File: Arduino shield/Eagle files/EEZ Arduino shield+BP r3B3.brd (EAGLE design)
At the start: 207 x 74 mm, 181 parts, among them IC21 TLC5925IDBQR, IC22 Si8641EC-B-IS1, IC23 SI8651EC-B-IS1, IC24 SI8651EC-B-IS1, IC25 LD1117ADT33TR, IC26 Si8641EC-B-IS1, IC27 PCA21125, IC28 AT25256B, IC29 W5500, IC30 BC857BS, IC31 TLC555, IC32 SN74LVC2G08DCTR, IC33 TPS3705-33D, IC34 SN74LV1T34DBVR, IC35 SN74LVC2G02DCTR, J1 BS-244DSM-R, J2 BS-244DSM-G, J3 BS-244DSM-B, J4 BS-244DSM-R, J5 BS-244DSM-B, Q23 IRLML2246TRPBF, Q24 IRLML2246TRPBF, Q25 IRLML2246TRPBF, Q26 IRLML2246TRPBF, Q27 2N7002, Q28 IRLML2246TRPBF, Q29 2N7002, Q30 2N7002, SW1 A101SYCQ04, SW2 1301.9316, X12 MC000006, X13 TSW-113-07-F-D, X14 MC000005, X15 TSW-113-07-F-D, X16 09185067324, X17 22-23-2021, X18 826629-8, X19 22-23-2041, X20 SSW-105-02-S-D, Y1 32,768kHz, Y2 25MHz

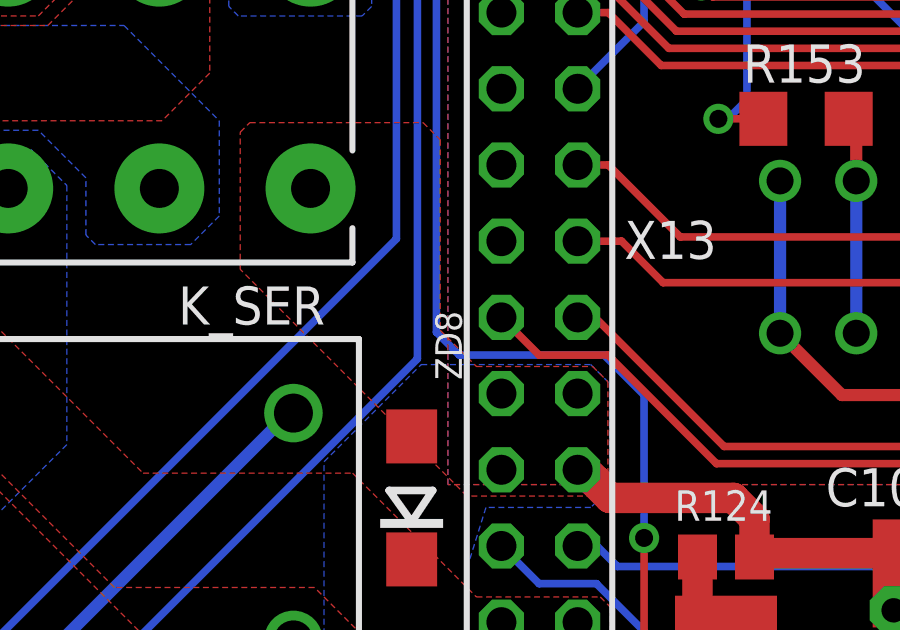
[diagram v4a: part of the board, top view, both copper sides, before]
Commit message: Missed hole added to Power board, minor bottom silk mask changes
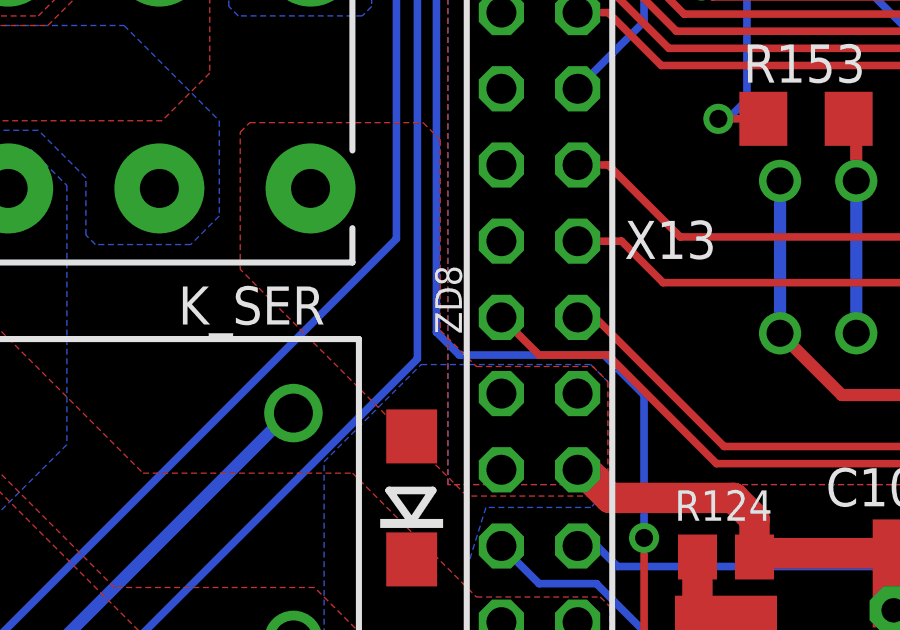
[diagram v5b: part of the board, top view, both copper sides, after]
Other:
- board text removed: "Licensed under the TAPR Open Hardware License (www.tapr.org/OHL)"

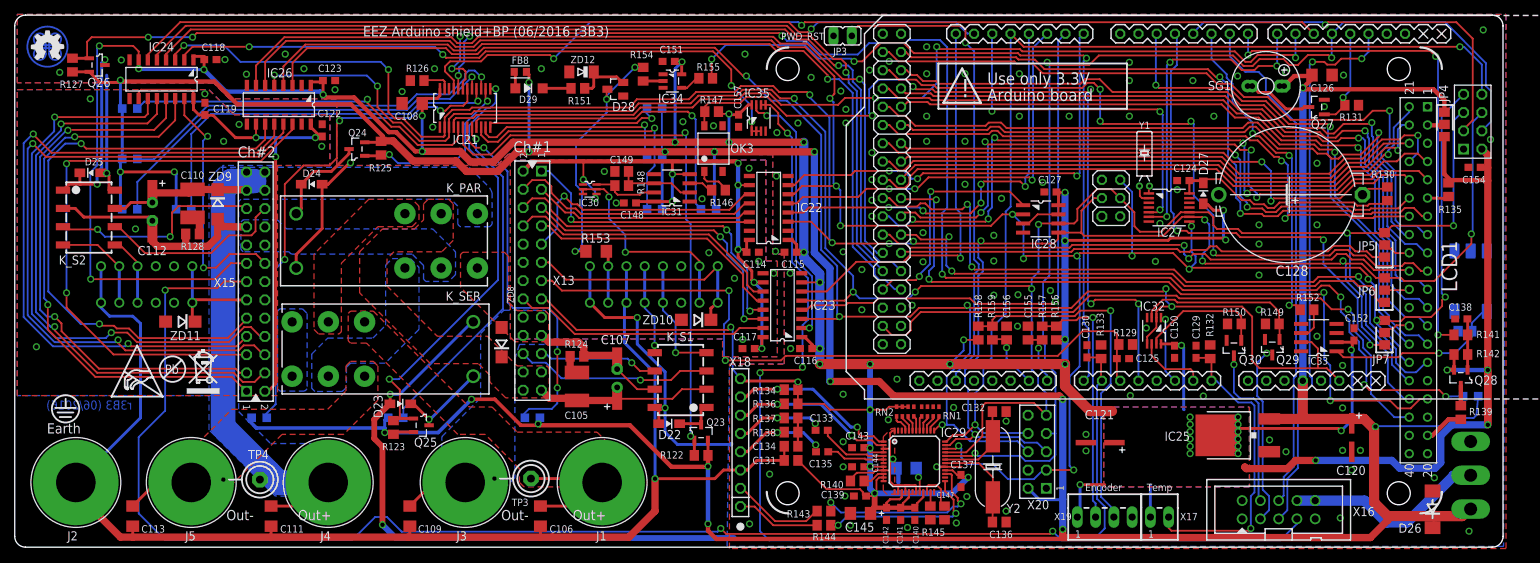
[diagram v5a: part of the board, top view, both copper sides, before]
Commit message: PCB fiducials, outlines, milling bridges
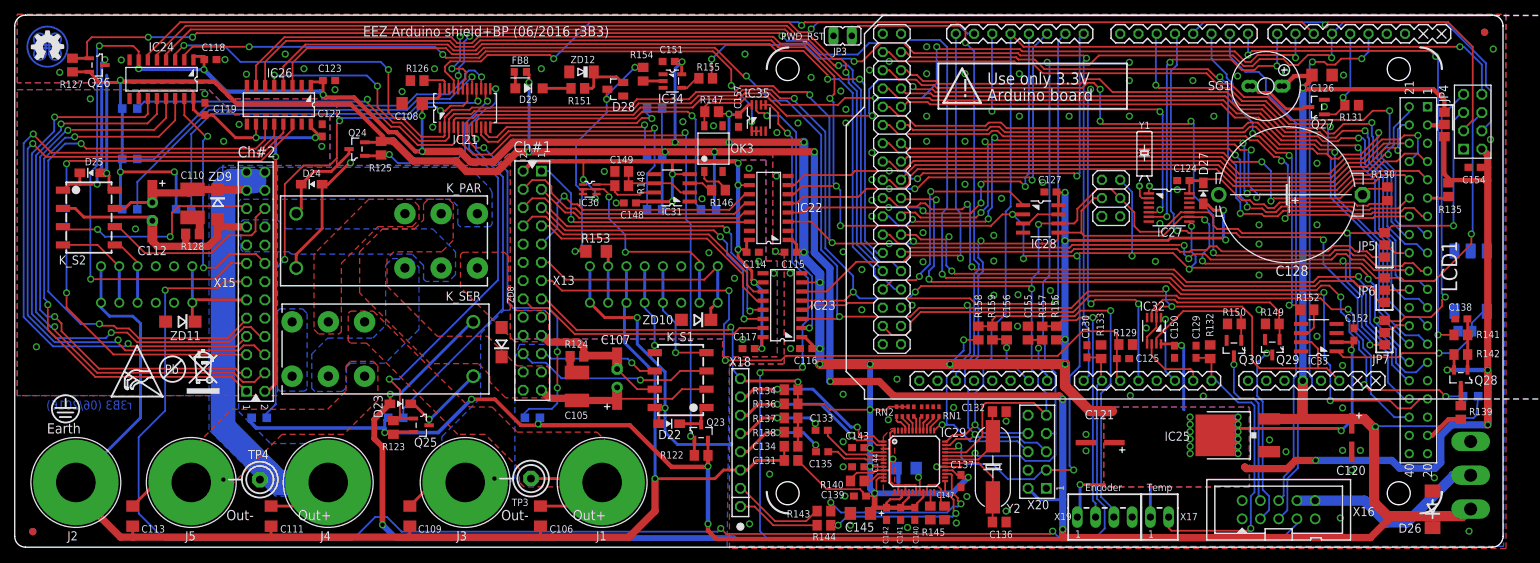
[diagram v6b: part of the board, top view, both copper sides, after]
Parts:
- added U$15, U$16: FIDUCIAL_2, EEZ_Lib1:FIDUCIAL_DUAL
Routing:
- net WIFI_CE: track 54.2 -> 53.5 mm
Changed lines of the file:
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@@
 <layer number="21" name="tPlace" color="7" fill="1" visible="yes" active="yes"/>
 <layer number="22" name="bPlace" color="13" fill="1" visible="no" active="yes"/>
-<layer number="23" name="tOrigins" color="15" fill="1" visible="no" active="yes"/>
+<layer number="23" name="tOrigins" color="15" fill="1" visible="yes" active="yes"/>
 <layer number="24" name="bOrigins" color="15" fill="1" visible="no" active="yes"/>
 <layer number="25" name="tNames" color="7" fill="1" visible="yes" active="yes"/>
@@
 <wire x1="152.781" y1="26.162" x2="152.781" y2="23.8125" width="2.54" layer="30"/>
 <text x="254.889" y="7.8105" size="1.016" layer="21" ratio="10" rot="R90">1</text>
-<dimension x1="316" y1="0" x2="109" y2="-1" x3="212.5" y3="-6.5" layer="113" dtype="horizontal"/>
+<dimension x1="316" y1="0" x2="109" y2="-1" x3="212.5" y3="-10.5" layer="47" dtype="horizontal"/>
 <dimension x1="301.5" y1="9.5" x2="216.5" y2="10" x3="259" y3="-5" layer="47" dtype="horizontal"/>
 <dimension x1="138.714" y1="21.7" x2="147.2" y2="0" x3="140.3145" y3="10.85" layer="47" dtype="vertical"/>
@@
 <text x="130.5980125" y="28.781503125" size="1.27" layer="125" ratio="10">ZD11</text>
 <text x="186.309" y="67.31" size="1.016" layer="125" ratio="10">ZD12</text>
-<dimension x1="109" y1="74" x2="108" y2="0" x3="105.5" y3="37" layer="113" dtype="vertical"/>
 </plain>
 <attributes>
@@
 <attribute name="NAME" x="312.4895" y="42.624" size="1.016" layer="26" ratio="10" rot="SMR0"/>
 </element>
+<element name="U$15" library="EEZ_Lib1" package="FIDUCIAL_DUAL" value="FIDUCIAL_2" x="313.436" y="71.628"/>
+<element name="U$16" library="EEZ_Lib1" package="FIDUCIAL_DUAL" value="FIDUCIAL_2" x="111.506" y="2.159"/>
 </elements>
 <signals>
@@
 <wire x1="238.379" y1="11.176" x2="240.7285" y2="11.176" width="0.254" layer="1"/>
 <via x="216.916" y="27.6225" extent="1-16" drill="0.6" shape="octagon"/>
-<via x="313.2455" y="71.9455" extent="1-16" drill="0.6" shape="octagon"/>
+<via x="314.6425" y="69.2785" extent="1-16" drill="0.6" shape="octagon"/>
 <via x="293.6875" y="13.462" extent="1-16" drill="0.6" shape="octagon"/>
 <via x="258.0005" y="15.6845" extent="1-16" drill="0.6" shape="octagon"/>
@@
 <wire x1="274.3708" y1="73.0123" x2="290.8935" y2="73.0123" width="0.254" layer="16"/>
 <via x="291.2745" y="72.644" extent="1-16" drill="0.6" shape="octagon"/>
-<wire x1="291.6555" y1="73.0123" x2="309.5117" y2="73.0123" width="0.254" layer="1"/>
+<wire x1="291.6555" y1="73.0123" x2="308.3687" y2="73.0123" width="0.254" layer="1"/>
 <wire x1="310.515" y1="57.912" x2="310.515" y2="58.1025" width="0.254" layer="1"/>
 <wire x1="310.515" y1="58.1025" x2="311.785" y2="59.3725" width="0.254" layer="1"/>
-<wire x1="311.785" y1="59.3725" x2="311.785" y2="70.739" width="0.254" layer="1"/>
+<wire x1="311.785" y1="59.3725" x2="311.785" y2="69.596" width="0.254" layer="1"/>
 <wire x1="291.6555" y1="73.0123" x2="291.2745" y2="72.644" width="0.254" layer="1"/>
 <wire x1="290.8935" y1="73.0123" x2="291.2745" y2="72.644" width="0.254" layer="16"/>
-<wire x1="309.5117" y1="73.0123" x2="311.785" y2="70.739" width="0.254" layer="1"/>
 <wire x1="274.3708" y1="73.0123" x2="272.912" y2="71.5535" width="0.254" layer="16"/>
 <wire x1="272.912" y1="71.412" x2="272.912" y2="71.5535" width="0.254" layer="16"/>
+<wire x1="308.3687" y1="73.0123" x2="311.785" y2="69.596" width="0.254" layer="1"/>
 </signal>
 <signal name="N$132">
